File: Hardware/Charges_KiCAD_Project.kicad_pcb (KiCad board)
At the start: 4 copper layers, 80 x 90.2 mm, 44 parts, among them IC1 TP124005-2, IC2 STM32L562VET6Q, J1 796684-4, J2 796684-4, J3 L717SDC37P1ACH4F, Q1 SI7232DN-T1-GE3, Q2 SI7232DN-T1-GE3, U1 MS5607-02BA, Y1 32mhz

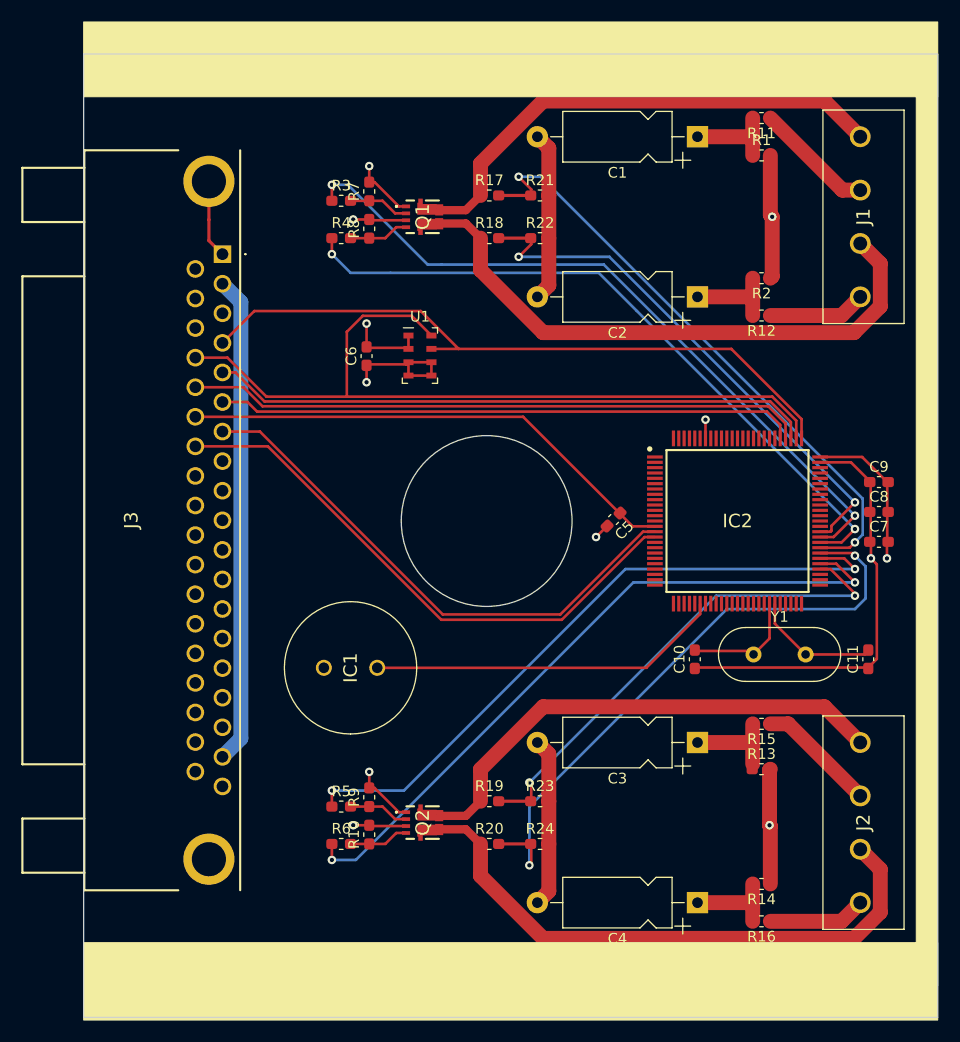
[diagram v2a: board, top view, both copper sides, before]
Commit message: update to caps and board layout
caps were changed and resistors were removed as they were not needed
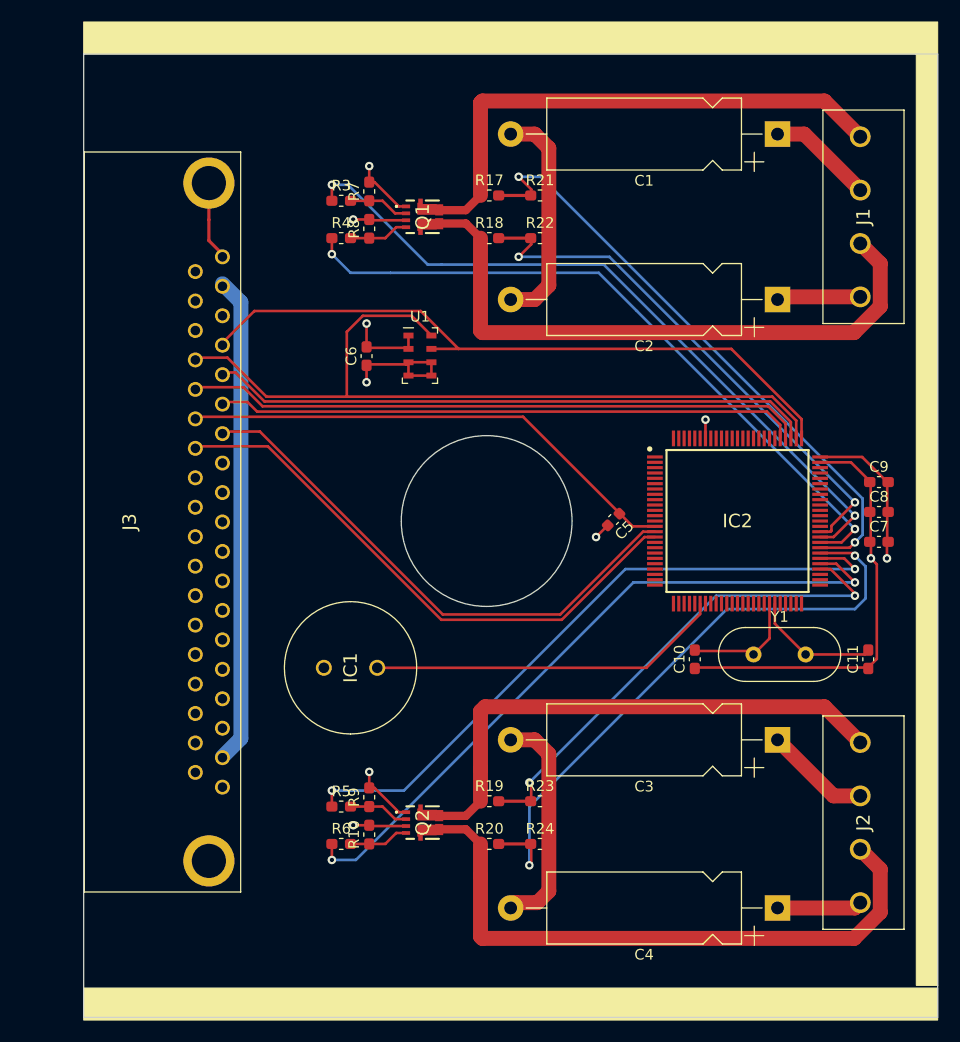
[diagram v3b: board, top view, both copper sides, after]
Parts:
- removed R1, R13, R14, R2: 10, Resistor_SMD:R_0603_1608Metric_Pad1.05x0.95mm_HandSolder
- removed R11, R12, R15, R16: 0.25, Resistor_SMD:R_0603_1608Metric_Pad1.05x0.95mm_HandSolder
- C1, C2, C3, C4: footprint Capacitor_THT:CP_Axial_L10.0mm_D4.5mm_P15.00mm_Horizontal -> Capacitor_THT:CP_Axial_L18.0mm_D6.5mm_P25.00mm_Horizontal
- C5: footprint Capacitor_SMD:C_0603_1608Metric_Pad1.08x0.95mm_HandSolder -> Capacitor_SMD:C_0603_1608Metric
- J3: value L717SDC37P1ACH4F -> D37S13A4GX00LF; footprint SamacSys_Parts:L717SDC37P1ACH4F -> SamacSys_Parts:D37S13A4GX00LF
- moved C4 7.52 mm to (153.5, 132.5)
- moved C1 7.50 mm to (153.5, 60.0)
- moved C2 7.50 mm to (153.5, 75.5)
- moved C3 7.50 mm to (153.5, 116.8)
- moved J3 0.25 mm to (101.5, 71.5)
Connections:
- C1 pad 1: Net-(C1-Pad1) -> +5V
- C2 pad 1: Net-(C2-Pad1) -> +5V
- C3 pad 1: Net-(C3-Pad1) -> +5V
- C4 pad 1: Net-(C4-Pad1) -> +5V
- IC2 pad 1: Net-(IC2-Pad1) -> (no net)
- IC2 pad 10: Net-(IC2-Pad10) -> (no net)
- IC2 pad 100: Net-(IC2-Pad100) -> (no net)
- IC2 pad 11: Net-(IC2-Pad11) -> (no net)
- IC2 pad 12: Net-(IC2-Pad12) -> (no net)
- IC2 pad 13: Net-(IC2-Pad13) -> (no net)
- IC2 pad 17: Net-(IC2-Pad17) -> (no net)
- IC2 pad 18: Net-(IC2-Pad18) -> (no net)
- IC2 pad 19: Net-(IC2-Pad19) -> (no net)
- IC2 pad 2: Net-(IC2-Pad2) -> (no net)
- IC2 pad 20: Net-(IC2-Pad20) -> (no net)
- IC2 pad 21: Net-(IC2-Pad21) -> (no net)
- IC2 pad 22: Net-(IC2-Pad22) -> (no net)
- IC2 pad 23: Net-(IC2-Pad23) -> (no net)
- IC2 pad 24: Net-(IC2-Pad24) -> (no net)
- IC2 pad 25: Net-(IC2-Pad25) -> (no net)
- IC2 pad 26: Net-(IC2-Pad26) -> (no net)
- IC2 pad 27: Net-(IC2-Pad27) -> (no net)
- IC2 pad 28: Net-(IC2-Pad28) -> (no net)
- IC2 pad 29: Net-(IC2-Pad29) -> (no net)
- IC2 pad 3: Net-(IC2-Pad3) -> (no net)
- IC2 pad 30: Net-(IC2-Pad30) -> (no net)
- IC2 pad 32: Net-(IC2-Pad32) -> (no net)
- IC2 pad 33: Net-(IC2-Pad33) -> (no net)
- IC2 pad 34: Net-(IC2-Pad34) -> (no net)
- IC2 pad 35: Net-(IC2-Pad35) -> (no net)
- IC2 pad 36: Net-(IC2-Pad36) -> (no net)
- IC2 pad 37: Net-(IC2-Pad37) -> (no net)
- IC2 pad 38: Net-(IC2-Pad38) -> (no net)
- IC2 pad 39: Net-(IC2-Pad39) -> (no net)
- IC2 pad 4: Net-(IC2-Pad4) -> (no net)
- IC2 pad 40: Net-(IC2-Pad40) -> (no net)
- IC2 pad 41: Net-(IC2-Pad41) -> (no net)
- IC2 pad 42: Net-(IC2-Pad42) -> (no net)
- IC2 pad 43: Net-(IC2-Pad43) -> (no net)
- IC2 pad 46: Net-(IC2-Pad46) -> (no net)
- IC2 pad 47: Net-(IC2-Pad47) -> (no net)
- IC2 pad 48: Net-(IC2-Pad48) -> (no net)
- IC2 pad 49: Net-(IC2-Pad49) -> (no net)
- IC2 pad 5: Net-(IC2-Pad5) -> (no net)
- IC2 pad 50: Net-(IC2-Pad50) -> (no net)
- IC2 pad 51: Net-(IC2-Pad51) -> (no net)
- IC2 pad 52: Net-(IC2-Pad52) -> (no net)
- IC2 pad 53: Net-(IC2-Pad53) -> (no net)
- IC2 pad 6: Net-(IC2-Pad6) -> (no net)
- IC2 pad 62: Net-(IC2-Pad62) -> (no net)
- IC2 pad 63: Net-(IC2-Pad63) -> (no net)
- IC2 pad 64: Net-(IC2-Pad64) -> (no net)
- IC2 pad 65: Net-(IC2-Pad65) -> (no net)
- IC2 pad 66: Net-(IC2-Pad66) -> (no net)
- IC2 pad 67: Net-(IC2-Pad67) -> (no net)
- IC2 pad 68: Net-(IC2-Pad68) -> (no net)
- IC2 pad 69: Net-(IC2-Pad69) -> (no net)
- IC2 pad 7: Net-(IC2-Pad7) -> (no net)
- IC2 pad 70: Net-(IC2-Pad70) -> (no net)
- IC2 pad 71: Net-(IC2-Pad71) -> (no net)
- IC2 pad 72: Net-(IC2-Pad72) -> (no net)
- IC2 pad 73: Net-(IC2-Pad73) -> (no net)
- IC2 pad 8: Net-(IC2-Pad8) -> (no net)
- IC2 pad 81: Net-(IC2-Pad81) -> (no net)
- IC2 pad 82: Net-(IC2-Pad82) -> (no net)
- IC2 pad 83: Net-(IC2-Pad83) -> (no net)
- IC2 pad 84: Net-(IC2-Pad84) -> (no net)
- IC2 pad 85: Net-(IC2-Pad85) -> (no net)
- IC2 pad 86: Net-(IC2-Pad86) -> (no net)
- IC2 pad 87: Net-(IC2-Pad87) -> (no net)
- IC2 pad 88: Net-(IC2-Pad88) -> (no net)
- IC2 pad 89: Net-(IC2-Pad89) -> (no net)
- IC2 pad 9: Net-(IC2-Pad9) -> (no net)
- IC2 pad 90: Net-(IC2-Pad90) -> (no net)
- IC2 pad 91: Net-(IC2-Pad91) -> (no net)
- IC2 pad 92: Net-(IC2-Pad92) -> (no net)
- IC2 pad 93: Net-(IC2-Pad93) -> (no net)
- IC2 pad 95: Net-(IC2-Pad95) -> (no net)
- IC2 pad 96: Net-(IC2-Pad96) -> (no net)
- IC2 pad 97: Net-(IC2-Pad97) -> (no net)
- IC2 pad 98: Net-(IC2-Pad98) -> (no net)
- IC2 pad 99: Net-(IC2-Pad99) -> (no net)
- J1 pad 2: Net-(J1-Pad2) -> +5V
- J1 pad 4: Net-(J1-Pad4) -> +5V
- J2 pad 2: Net-(J2-Pad2) -> +5V
- J2 pad 4: Net-(J2-Pad4) -> +5V
- J3 pad 10: Net-(J3-Pad10) -> (no net)
- J3 pad 11: Net-(J3-Pad11) -> (no net)
- J3 pad 12: Net-(J3-Pad12) -> (no net)
- J3 pad 13: Net-(J3-Pad13) -> (no net)
- J3 pad 14: Net-(J3-Pad14) -> (no net)
- J3 pad 15: Net-(J3-Pad15) -> (no net)
- J3 pad 16: Net-(J3-Pad16) -> (no net)
- J3 pad 17: Net-(J3-Pad17) -> (no net)
- J3 pad 21: /DSUB_37_Male/t_mosi -> (no net)
- J3 pad 22: /DSUB_37_Male/t_clk -> (no net)
- J3 pad 27: Net-(J3-Pad27) -> (no net)
- J3 pad 28: Net-(J3-Pad28) -> (no net)
- J3 pad 29: Net-(J3-Pad29) -> (no net)
- J3 pad 3: /DSUB_37_Male/t_miso -> (no net)
- J3 pad 30: Net-(J3-Pad30) -> (no net)
- J3 pad 31: Net-(J3-Pad31) -> (no net)
- J3 pad 32: Net-(J3-Pad32) -> (no net)
- J3 pad 33: Net-(J3-Pad33) -> (no net)
- J3 pad 34: Net-(J3-Pad34) -> (no net)
- J3 pad 35: Net-(J3-Pad35) -> (no net)
- J3 pad 36: Net-(J3-Pad36) -> (no net)
- J3 pad 8: Net-(J3-Pad8) -> (no net)
- J3 pad 9: Net-(J3-Pad9) -> (no net)
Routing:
- net +5V: track 22.5 -> 35.7 mm, vias 2 -> 0
- net Net-(J2-Pad2): track 11.2 -> 0.00 mm
- net Net-(J1-Pad2): track 11.2 -> 0.00 mm
- net GND: track 116.3 -> 126.8 mm
- net Net-(J2-Pad4): track 9.15 -> 0.00 mm
- net Net-(J1-Pad4): track 9.15 -> 0.00 mm
- net Net-(C3-Pad1): track 9.00 -> 0.00 mm
- net Net-(C2-Pad1): track 8.71 -> 0.00 mm
- net Net-(C1-Pad1): track 8.71 -> 0.00 mm
- net Net-(C4-Pad1): track 8.71 -> 0.00 mm
- net /Fet_D: track 55.6 -> 58.9 mm
- net /Fet_B: track 55.6 -> 58.9 mm
- net /Fet_A: track 47.4 -> 50.7 mm
- net /Fet_C: track 47.4 -> 50.6 mm

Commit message: Added qr codes and fixed silk screen
Qr code was added and the silk screens were fixed. corners were also rounded
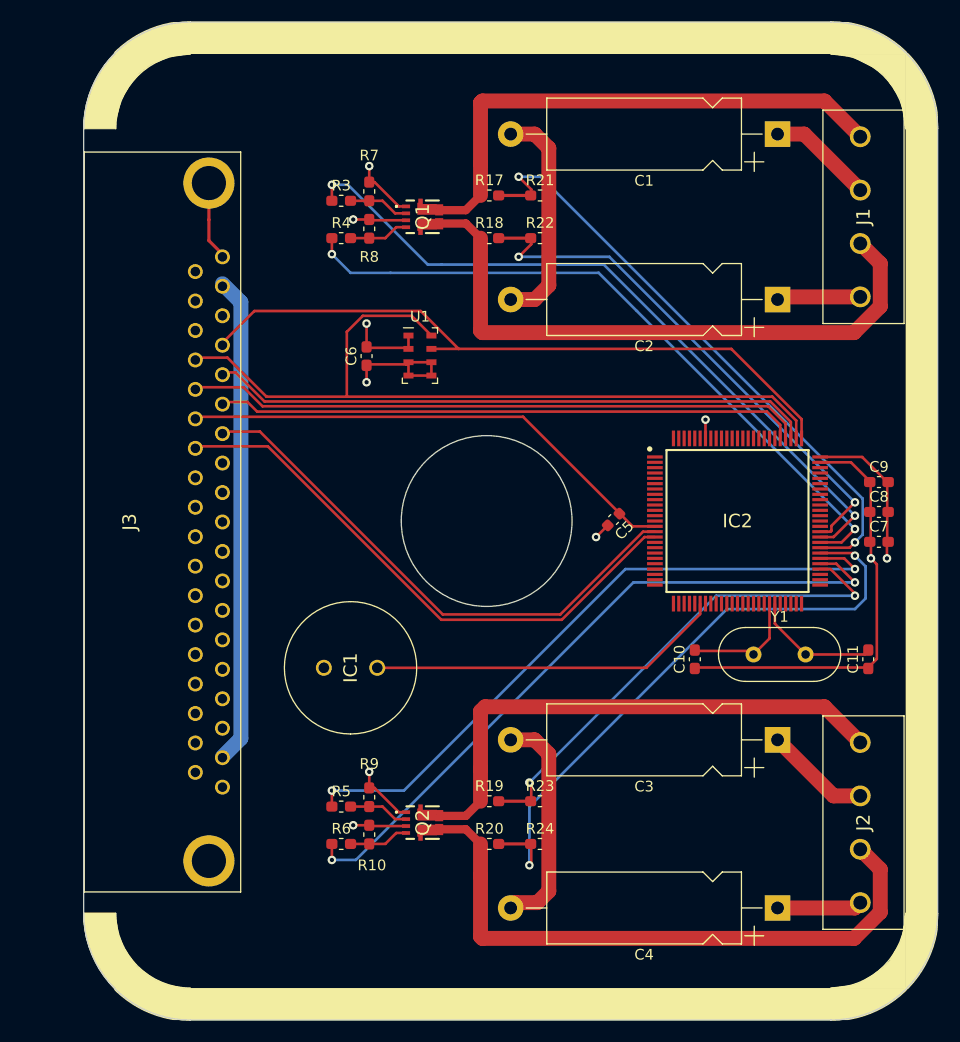
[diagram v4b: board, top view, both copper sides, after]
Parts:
- added G***: LOGO, RDT_Custom_Footprints:charges_qr_code, B.Cu at (142.2, 126.8)
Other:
- board size 80 x 90.2 mm -> 80 x 93.5 mm

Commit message: Added signatures to silkscreen
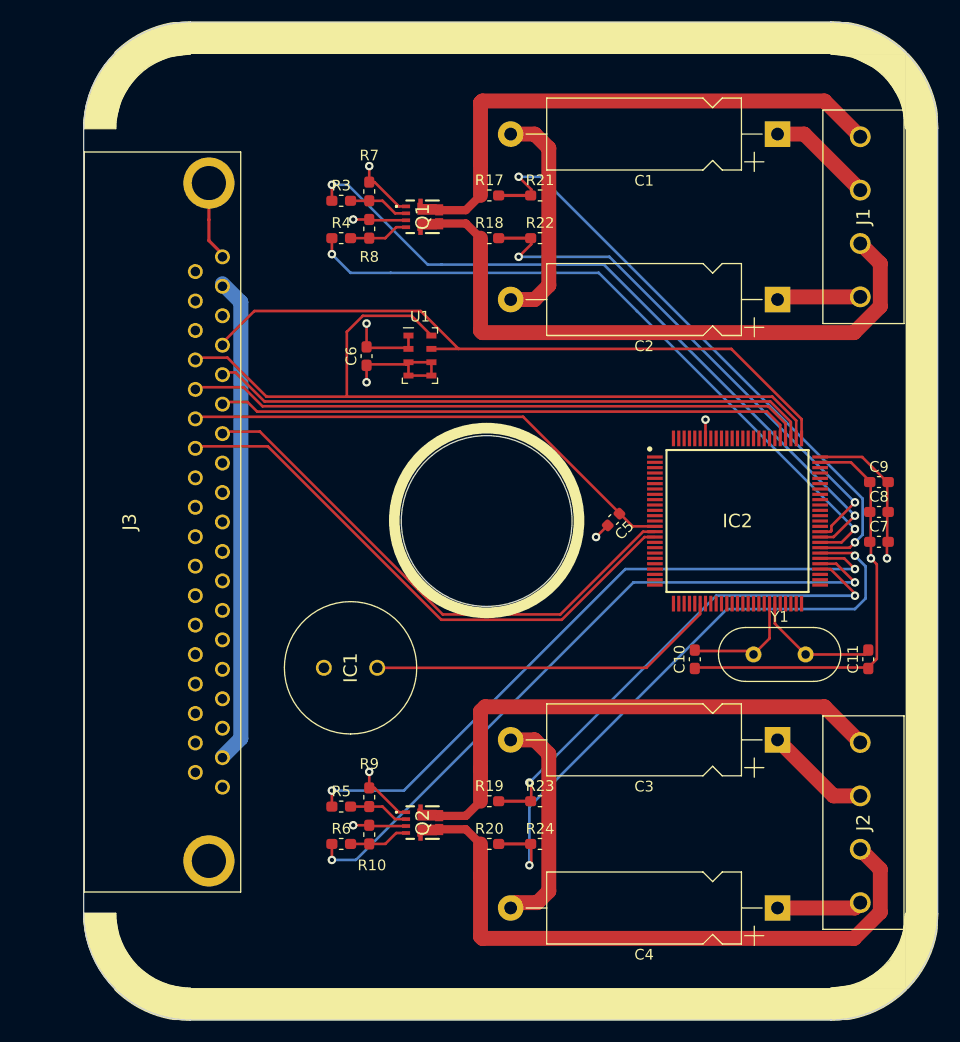
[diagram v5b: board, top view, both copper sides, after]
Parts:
- added G***: LOGO, Custom_Graphics:ThomasFSignature, B.Cu at (127.7, 59.7)
- added G***: LOGO, Graphics:JacobKSignature, B.Cu at (127.6, 133.8)
- added G***: LOGO, Custom_Graphics:RDT_Logo, B.Cu at (111.0, 98.3)
- moved G*** 33.0 mm to (154.8, 96.2)
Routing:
- added copper zone on In2.Cu, net +5V
- added copper zone on In1.Cu, net GND
- removed copper zone on power, net +5V
- removed copper zone on Ground, net GND
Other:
- net class 1amp removed
- net class 5amp removed
- net class Default removed
- board text added: "Jacob King"
- board text added: "Thomas Francois KXØSTL"
